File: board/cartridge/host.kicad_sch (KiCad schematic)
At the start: 30 parts, among them P1 Card Edge, U13 74AHCV05, U4 TXS0108E, U5 74LVC245, U6 74LVC1G17, U7 74LS540, U8 74LS540

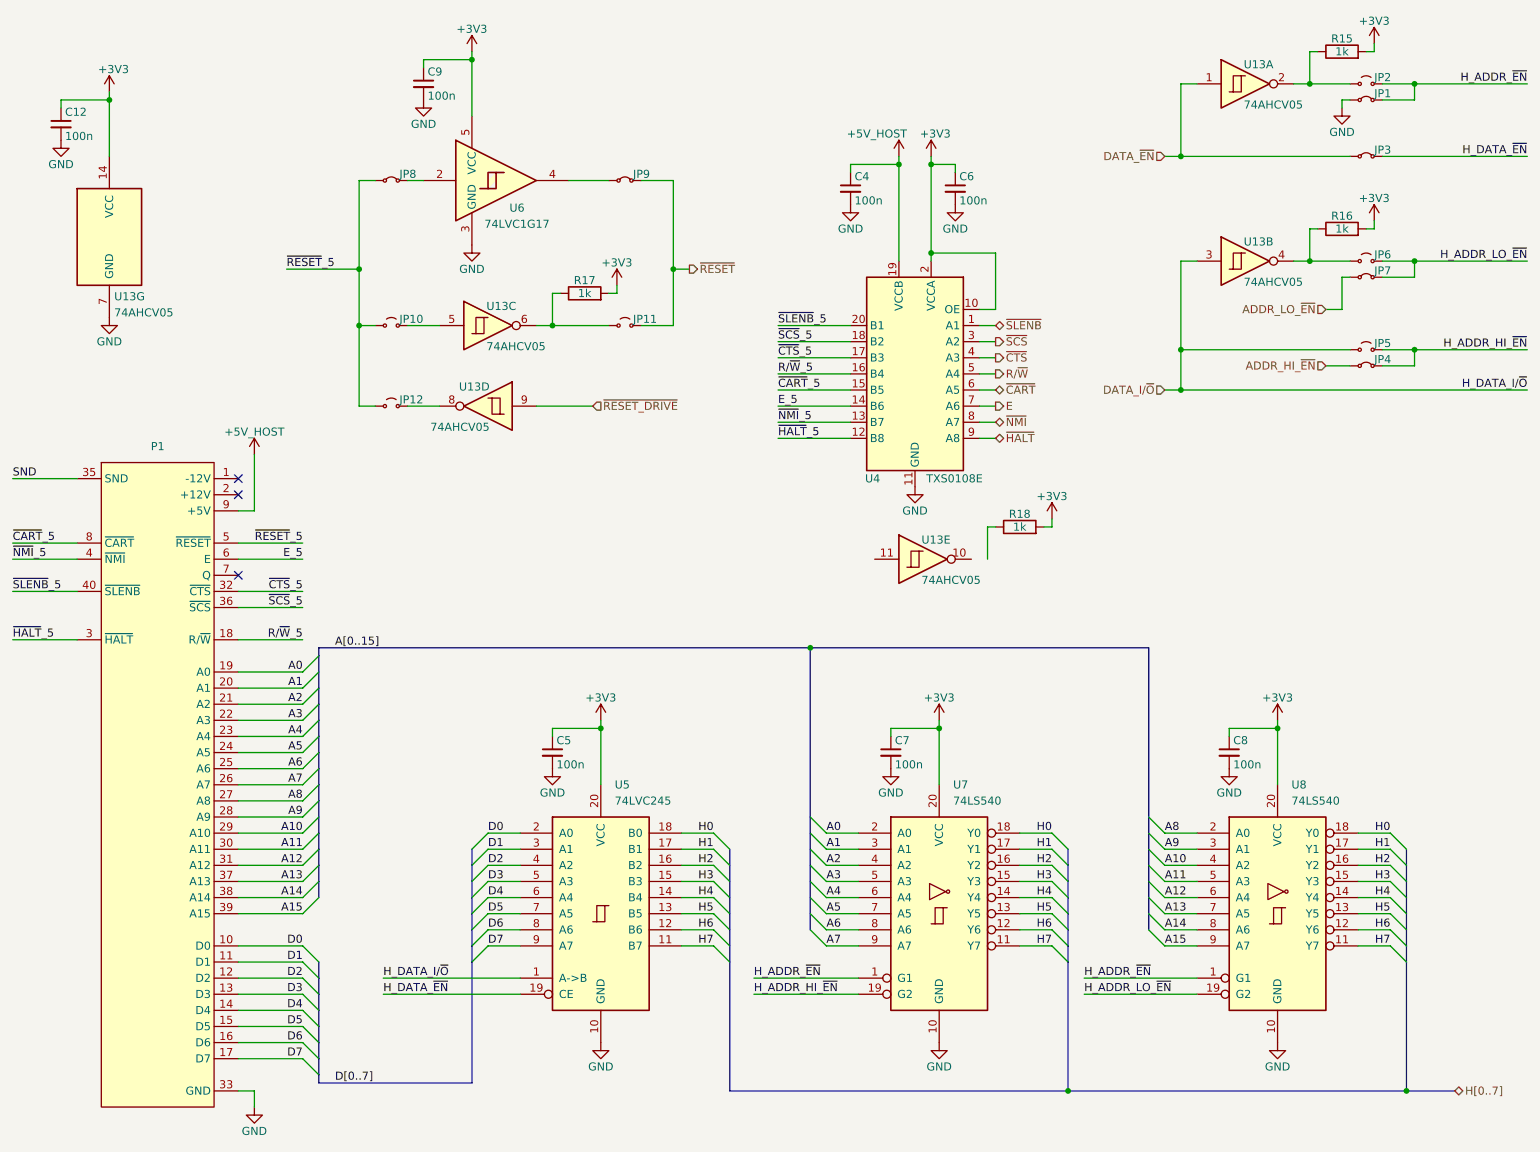
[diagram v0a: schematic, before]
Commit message: Finish adding solder links for configuration.
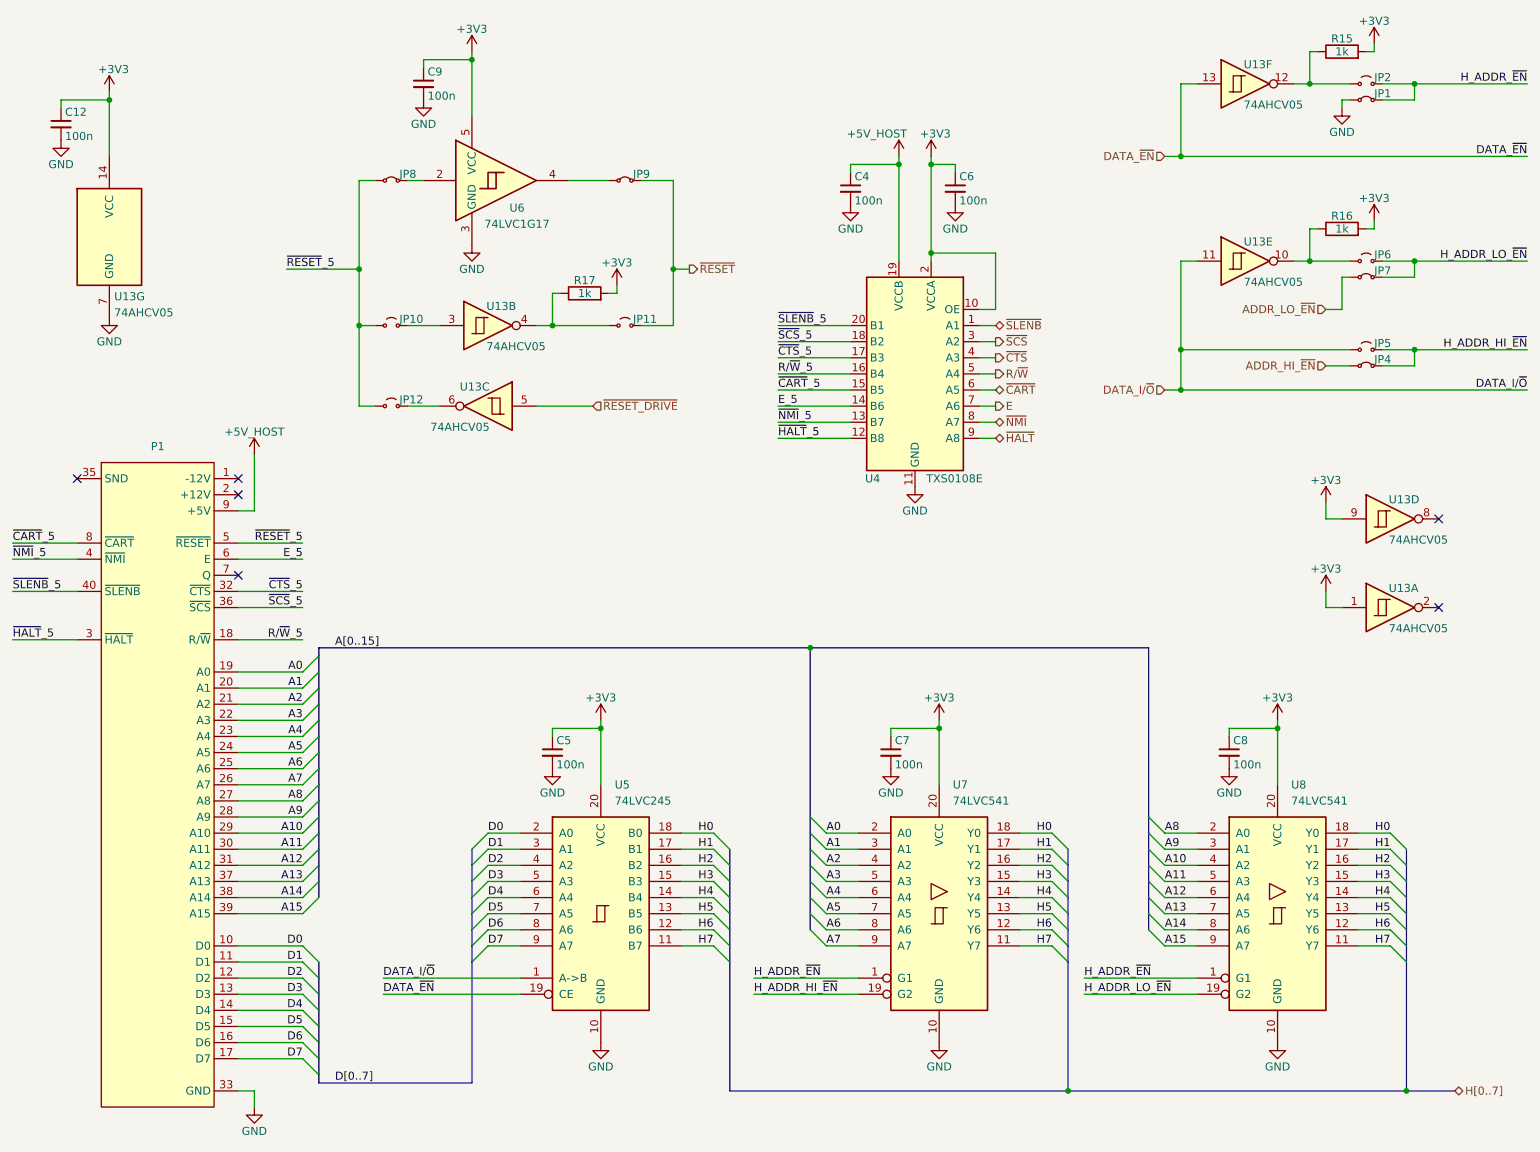
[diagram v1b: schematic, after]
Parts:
- removed JP3: Jumper_2_Small_Bridged, Jumper:SolderJumper-2_P1.3mm_Open_TrianglePad1.0x1.5mm, symbol Jumper:Jumper_2_Small_Bridged
- removed R18: 1k, Resistor_SMD:R_0603_1608Metric, symbol Device:R
- added unit 1 of U13
- U7, U8: value 74LS540 -> 74LVC541; footprint (none) -> Package_SO:TSSOP-20_4.4x6.5mm_P0.65mm; symbol 74xx:74LS540 -> 74xx:74LS541
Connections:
- net H_DATA_~{EN} is gone; now on net DATA_~{EN}: U5.19 (CE)
- net +3V3: now also U13.9, U13.1
- net DATA_I/~{O}: now also U13.11; no longer U13.3
- net DATA_~{EN}: now also U13.13; no longer U13.1
- net ~{RESET_DRIVE}: now also U13.5; no longer U13.9
- net at JP12.2 (B): now also U13.6; no longer U13.8
- net at JP2.1 (A), R15.1: now also U13.12; no longer U13.2
- net at JP10.2 (B): now also U13.3; no longer U13.5
- net at JP6.1 (A), R16.1: now also U13.10; no longer U13.4
- net at JP11.1 (A), R17.1: now also U13.4; no longer U13.6
- net SND: no longer names the net of P1.35 (SND)
- no-connect marks 3 -> 6
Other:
- company: © 2023-2024 Sam Hanes, licensed CERN-OHL-W v2 -> © 2023-2025 Sam Hanes, licensed CERN-OHL-W v2
- moved on the sheet: U13D

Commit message: Ensure all parts are available from DigiKey and JLCPCB.
This switches the symbols and footprints to the more widely available
parts sourced from DigiKey. Parts also have an LCSC catalog number,
which may be the same part or a cheaper compatible clone.
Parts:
- U13: DigiKey (none) -> 1727-8669-1-ND; LCSC (none) -> C554727
- U4: DigiKey (none) -> 296-23011-1-ND; LCSC (none) -> C17206
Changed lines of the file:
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@@
 			)
 		)
+		(property "LCSC" "C554727"
+			(at 233.68 96.52 0)
+			(effects
+				(font
+					(size 1.27 1.27)
+				)
+				(hide yes)
+			)
+		)
+		(property "DigiKey" "1727-8669-1-ND"
+			(at 233.68 96.52 0)
+			(effects
+				(font
+					(size 1.27 1.27)
+				)
+				(hide yes)
+			)
+		)
 		(pin "2"
 		)
@@
 			)
 		)
+		(property "LCSC" "C554727"
+			(at 210.82 27.94 0)
+			(effects
+				(font
+					(size 1.27 1.27)
+				)
+				(hide yes)
+			)
+		)
+		(property "DigiKey" "1727-8669-1-ND"
+			(at 210.82 27.94 0)
+			(effects
+				(font
+					(size 1.27 1.27)
+				)
+				(hide yes)
+			)
+		)
 		(pin "2"
 		)
@@
 			)
 		)
+		(property "LCSC" "C554727"
+			(at 233.68 110.49 0)
+			(effects
+				(font
+					(size 1.27 1.27)
+				)
+				(hide yes)
+			)
+		)
+		(property "DigiKey" "1727-8669-1-ND"
+			(at 233.68 110.49 0)
+			(effects
+				(font
+					(size 1.27 1.27)
+				)
+				(hide yes)
+			)
+		)
 		(pin "2"
 		)
@@
 			)
 		)
+		(property "LCSC" "C554727"
+			(at 91.44 78.74 0)
+			(effects
+				(font
+					(size 1.27 1.27)
+				)
+				(hide yes)
+			)
+		)
+		(property "DigiKey" "1727-8669-1-ND"
+			(at 91.44 78.74 0)
+			(effects
+				(font
+					(size 1.27 1.27)
+				)
+				(hide yes)
+			)
+		)
 		(pin "2"
 		)
@@
 			)
 		)
+		(property "LCSC" "C554727"
+			(at 91.44 66.04 0)
+			(effects
+				(font
+					(size 1.27 1.27)
+				)
+				(hide yes)
+			)
+		)
+		(property "DigiKey" "1727-8669-1-ND"
+			(at 91.44 66.04 0)
+			(effects
+				(font
+					(size 1.27 1.27)
+				)
+				(hide yes)
+			)
+		)
 		(pin "2"
 		)
@@
 			)
 		)
+		(property "LCSC" "C17206"
+			(at 158.75 73.66 0)
+			(effects
+				(font
+					(size 1.27 1.27)
+				)
+				(hide yes)
+			)
+		)
+		(property "DigiKey" "296-23011-1-ND"
+			(at 158.75 73.66 0)
+			(effects
+				(font
+					(size 1.27 1.27)
+				)
+				(hide yes)
+			)
+		)
 		(pin "13"
 		)
@@
 			)
 		)
+		(property "LCSC" "C554727"
+			(at 210.82 55.88 0)
+			(effects
+				(font
+					(size 1.27 1.27)
+				)
+				(hide yes)
+			)
+		)
+		(property "DigiKey" "1727-8669-1-ND"
+			(at 210.82 55.88 0)
+			(effects
+				(font
+					(size 1.27 1.27)
+				)
+				(hide yes)
+			)
+		)
 		(pin "2"
 		)
@@
 			)
 		)
-		(property "Description" "Octal BUS Transceivers, 3-State outputs"
+		(property "Description" "Octal BUS Transceivers, 3-State outputs, Schmitt-trigger inputs"
 			(at 109.22 158.75 0)
 			(effects
@@
 			(at 31.75 52.07 0)
 			(effects
+				(font
+					(size 1.27 1.27)
+				)
+				(hide yes)
+			)
+		)
+		(property "LCSC" "C554727"
+			(at 31.75 52.07 0)
+			(effects
+				(font
+					(size 1.27 1.27)
+				)
+				(hide yes)
+			)
+		)
+		(property "DigiKey" "1727-8669-1-ND"
+			(at 31.75 52.07 0)
+			(effects
